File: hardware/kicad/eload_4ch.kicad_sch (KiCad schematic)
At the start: 0 parts

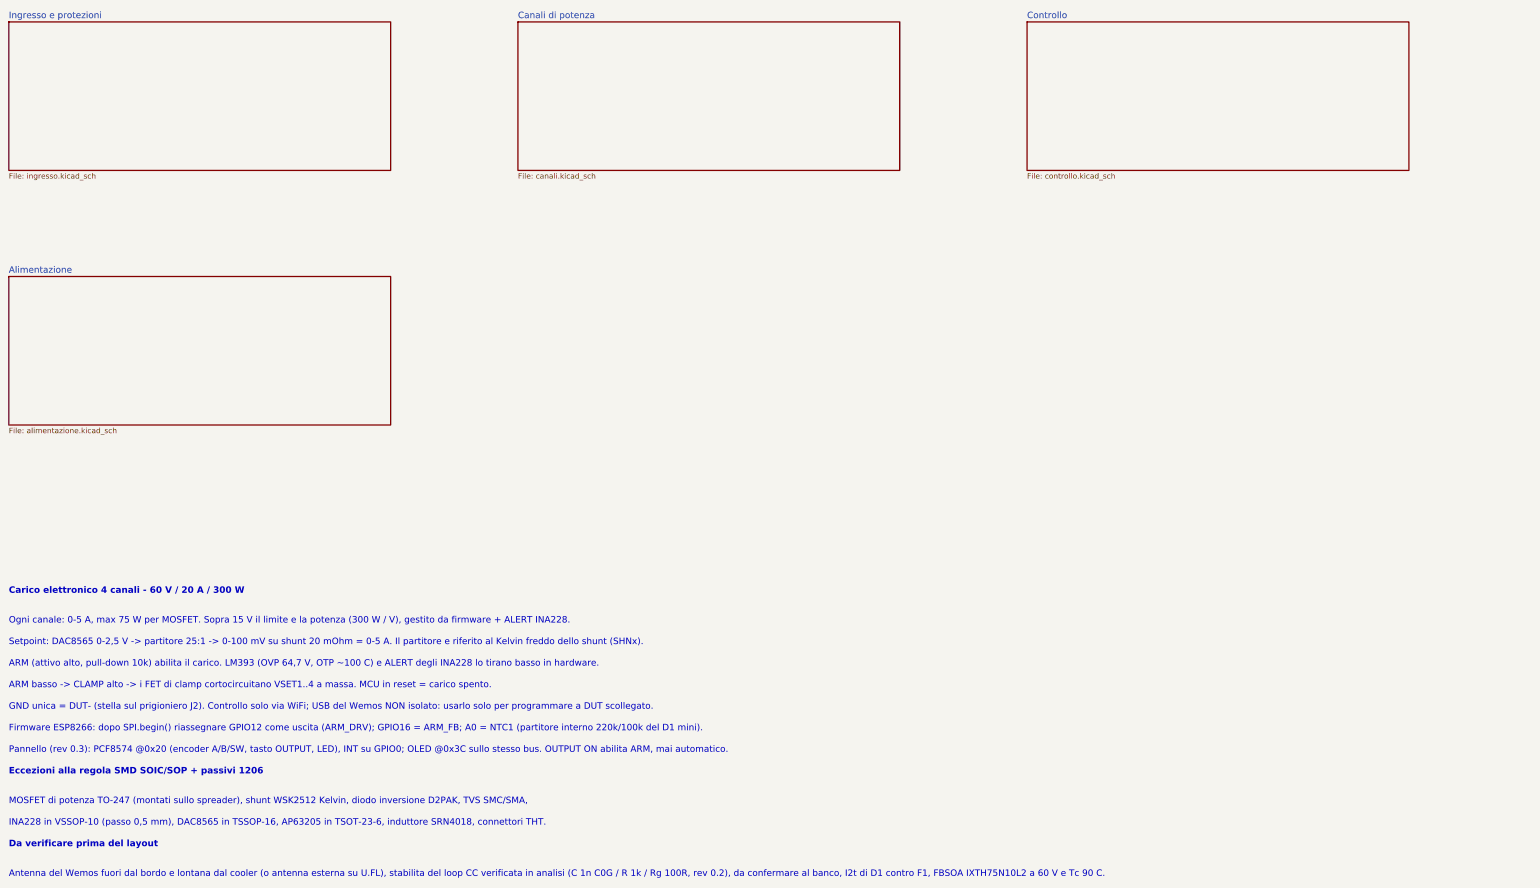
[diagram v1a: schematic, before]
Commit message: Translate schematic and PCB to English
Sheets renamed (input, channels, control, power), all titles, notes,
values and board texts in English; symbol library renamed to eload.
Re-routed board: DRC with schematic parity clean.

Co-Authored-By: Claude Opus 5.5 <noreply@anthropic.com>
Claude-Session: https://claude.ai/code/session_013KrwoEq2Y4F9LNKutY5RJ4
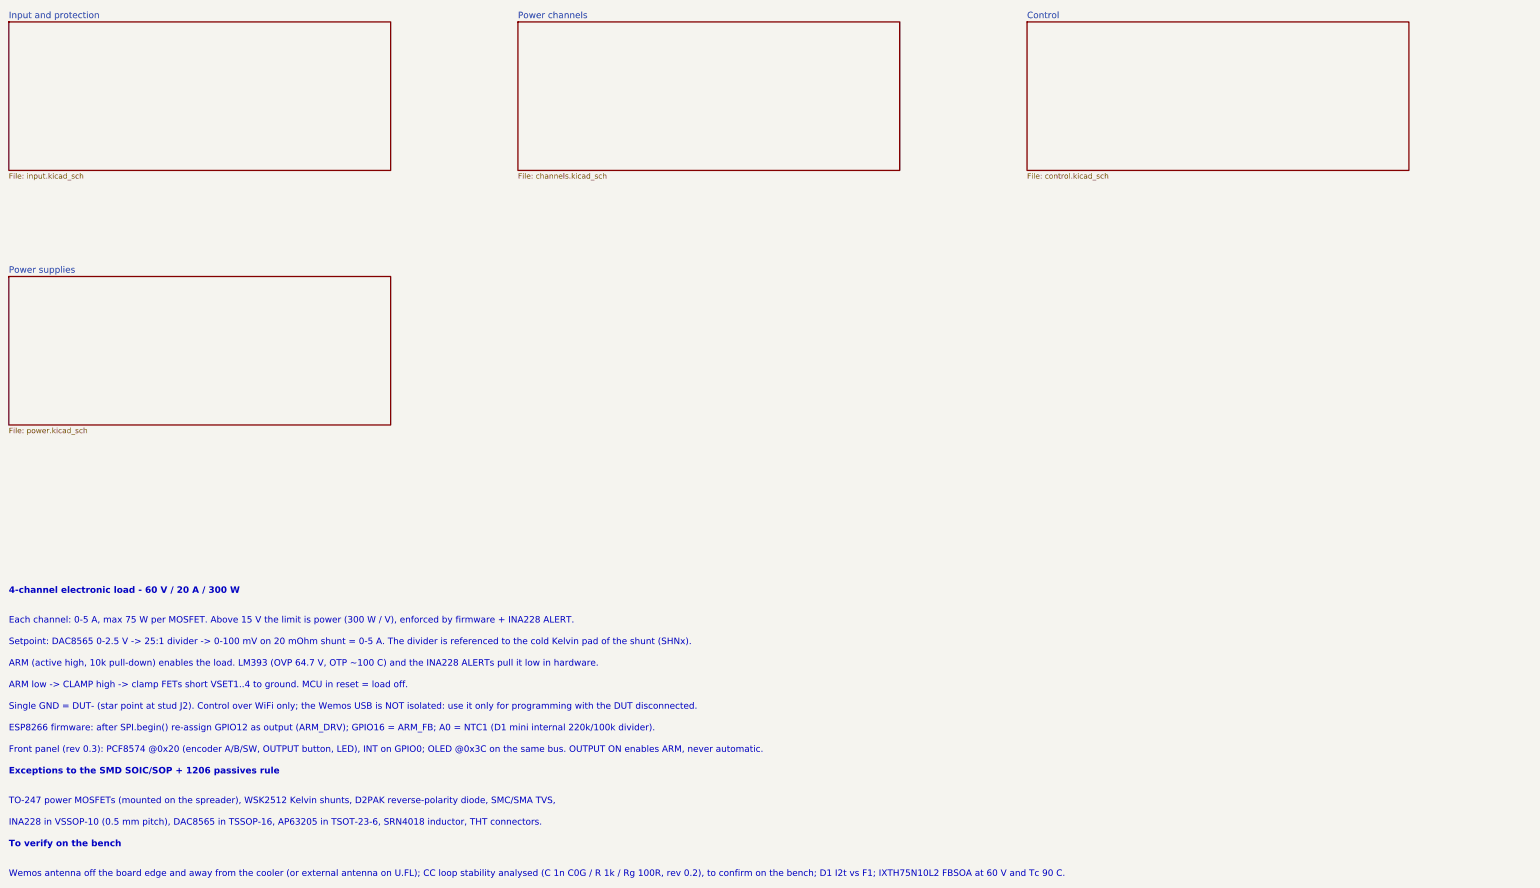
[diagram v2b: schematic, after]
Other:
- removed sheet Alimentazione
- removed sheet Canali di potenza
- removed sheet Controllo
- removed sheet Ingresso e protezioni
- added sheet Control (control.kicad_sch)
- added sheet Input and protection (input.kicad_sch)
- added sheet Power channels (channels.kicad_sch)
- added sheet Power supplies (power.kicad_sch)
- note added: "4-channel electronic load - 60 V / 20 A / 300 W"
- note added: "ARM (active high, 10k pull-down) enables the load. LM393 (OVP 64.7 V, OTP ~100 C) and the INA228 ALERTs pull it low in hardware."
- note added: "ARM low -> CLAMP high -> clamp FETs short VSET1..4 to ground. MCU in reset = load off."
- note added: "ESP8266 firmware: after SPI.begin() re-assign GPIO12 as output (ARM_DRV); GPIO16 = ARM_FB; A0 = NTC1 (D1 mini internal 220k/100k divider)."
- note added: "Each channel: 0-5 A, max 75 W per MOSFET. Above 15 V the limit is power (300 W / V), enforced by firmware + INA228 ALERT."
- note added: "Exceptions to the SMD SOIC/SOP + 1206 passives rule"
- note added: "Front panel (rev 0.3): PCF8574 @0x20 (encoder A/B/SW, OUTPUT button, LED), INT on GPIO0; OLED @0x3C on the same bus. OUTPUT ON enables ARM, never automatic."
- note added: "INA228 in VSSOP-10 (0.5 mm pitch), DAC8565 in TSSOP-16, AP63205 in TSOT-23-6, SRN4018 inductor, THT connectors."
- note added: "Setpoint: DAC8565 0-2.5 V -> 25:1 divider -> 0-100 mV on 20 mOhm shunt = 0-5 A. The divider is referenced to the cold Kelvin pad of the shunt (SHNx)."
- note added: "Single GND = DUT- (star point at stud J2). Control over WiFi only; the Wemos USB is NOT isolated: use it only for programming with the DUT disconnected."
- note added: "TO-247 power MOSFETs (mounted on the spreader), WSK2512 Kelvin shunts, D2PAK reverse-polarity diode, SMC/SMA TVS,"
- note added: "To verify on the bench"
- note added: "Wemos antenna off the board edge and away from the cooler (or external antenna on U.FL); CC loop stability analysed (C 1n C0G / R 1k / Rg 100R, rev 0.2), to confirm on the bench; D1 I2t vs F1; IXTH75N10L2 FBSOA at 60 V and Tc 90 C."
- note removed: "ARM (attivo alto, pull-down 10k) abilita il carico. LM393 (OVP 64,7 V, OTP ~100 C) e ALERT degli INA228 lo tirano basso in hardware."
- note removed: "ARM basso -> CLAMP alto -> i FET di clamp cortocircuitano VSET1..4 a massa. MCU in reset = carico spento."
- note removed: "Antenna del Wemos fuori dal bordo e lontana dal cooler (o antenna esterna su U.FL), stabilita del loop CC verificata in analisi (C 1n C0G / R 1k / Rg 100R, rev 0.2), da confermare al banco, I2t di D1 contro F1, FBSOA IXTH75N10L2 a 60 V e Tc 90 C."
- note removed: "Carico elettronico 4 canali - 60 V / 20 A / 300 W"
- note removed: "Da verificare prima del layout"
- note removed: "Eccezioni alla regola SMD SOIC/SOP + passivi 1206"
- note removed: "Firmware ESP8266: dopo SPI.begin() riassegnare GPIO12 come uscita (ARM_DRV); GPIO16 = ARM_FB; A0 = NTC1 (partitore interno 220k/100k del D1 mini)."
- note removed: "GND unica = DUT- (stella sul prigioniero J2). Controllo solo via WiFi; USB del Wemos NON isolato: usarlo solo per programmare a DUT scollegato."
- note removed: "INA228 in VSSOP-10 (passo 0,5 mm), DAC8565 in TSSOP-16, AP63205 in TSOT-23-6, induttore SRN4018, connettori THT."
- note removed: "MOSFET di potenza TO-247 (montati sullo spreader), shunt WSK2512 Kelvin, diodo inversione D2PAK, TVS SMC/SMA,"
- note removed: "Ogni canale: 0-5 A, max 75 W per MOSFET. Sopra 15 V il limite e la potenza (300 W / V), gestito da firmware + ALERT INA228."
- note removed: "Pannello (rev 0.3): PCF8574 @0x20 (encoder A/B/SW, tasto OUTPUT, LED), INT su GPIO0; OLED @0x3C sullo stesso bus. OUTPUT ON abilita ARM, mai automatico."
- note removed: "Setpoint: DAC8565 0-2,5 V -> partitore 25:1 -> 0-100 mV su shunt 20 mOhm = 0-5 A. Il partitore e riferito al Kelvin freddo dello shunt (SHNx)."
- title: Carico attivo 60V 20A 300W — Indice -> Electronic Load 4ch 60V 20A 300W — Index
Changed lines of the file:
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@@
 	(paper "A3")
 	(title_block
-		(title "Carico attivo 60V 20A 300W — Indice")
+		(title "Electronic Load 4ch 60V 20A 300W — Index")
 		(date "2026-10-25")
 		(rev "0.3")
 		(company "IV3HGA")
-		(comment 1 "Schema gerarchico: un foglio per blocco funzionale")
-	)
-	(text "GND unica = DUT- (stella sul prigioniero J2). Controllo solo via WiFi; USB del Wemos NON isolato: usarlo solo per programmare a DUT scollegato."
+		(comment 1 "Hierarchical schematic: one sheet per functional block")
+	)
+	(text "Exceptions to the SMD SOIC/SOP + 1206 passives rule"
+		(exclude_from_sim no)
+		(at 30 227.56 0)
+		(effects
+			(font
+				(size 1.524 1.524)
+				(bold yes)
+			)
+			(justify left bottom)
+		)
+	)
+	(text "INA228 in VSSOP-10 (0.5 mm pitch), DAC8565 in TSSOP-16, AP63205 in TSOT-23-6, SRN4018 inductor, THT connectors."
+		(exclude_from_sim no)
+		(at 30 239.64 0)
+		(effects
+			(font
+				(size 1.524 1.524)
+			)
+			(justify left bottom)
+		)
+	)
+	(text "4-channel electronic load - 60 V / 20 A / 300 W"
+		(exclude_from_sim no)
+		(at 30 185 0)
+		(effects
+			(font
+				(size 1.524 1.524)
+				(bold yes)
+			)
+			(justify left bottom)
+		)
+	)
+	(text "Setpoint: DAC8565 0-2.5 V -> 25:1 divider -> 0-100 mV on 20 mOhm shunt = 0-5 A. The divider is referenced to the cold Kelvin pad of the shunt (SHNx)."
+		(exclude_from_sim no)
+		(at 30 197.08 0)
+		(effects
+			(font
+				(size 1.524 1.524)
+			)
+			(justify left bottom)
+		)
+	)
+	(text "Wemos antenna off the board edge and away from the cooler (or external antenna on U.FL); CC loop stability analysed (C 1n C0G / R 1k / Rg 100R, rev 0.2), to confirm on the bench; D1 I2t vs F1; IXTH75N10L2 FBSOA at 60 V and Tc 90 C."
+		(exclude_from_sim no)
+		(at 30 251.72 0)
+		(effects
+			(font
+				(size 1.524 1.524)
+			)
+			(justify left bottom)
+		)
+	)
+	(text "ARM (active high, 10k pull-down) enables the load. LM393 (OVP 64.7 V, OTP ~100 C) and the INA228 ALERTs pull it low in hardware."
+		(exclude_from_sim no)
+		(at 30 202.16 0)
+		(effects
+			(font
+				(size 1.524 1.524)
+			)
+			(justify left bottom)
+		)
+	)
+	(text "Each channel: 0-5 A, max 75 W per MOSFET. Above 15 V the limit is power (300 W / V), enforced by firmware + INA228 ALERT."
+		(exclude_from_sim no)
+		(at 30 192 0)
+		(effects
+			(font
+				(size 1.524 1.524)
+			)
+			(justify left bottom)
+		)
+	)
+	(text "ARM low -> CLAMP high -> clamp FETs short VSET1..4 to ground. MCU in reset = load off."
+		(exclude_from_sim no)
+		(at 30 207.24 0)
+		(effects
+			(font
+				(size 1.524 1.524)
+			)
+			(justify left bottom)
+		)
+	)
+	(text "ESP8266 firmware: after SPI.begin() re-assign GPIO12 as output (ARM_DRV); GPIO16 = ARM_FB; A0 = NTC1 (D1 mini internal 220k/100k divider)."
+		(exclude_from_sim no)
+		(at 30 217.4 0)
+		(effects
+			(font
+				(size 1.524 1.524)
+			)
+			(justify left bottom)
+		)
+	)
+	(text "Front panel (rev 0.3): PCF8574 @0x20 (encoder A/B/SW, OUTPUT button, LED), INT on GPIO0; OLED @0x3C on the same bus. OUTPUT ON enables ARM, never automatic."
+		(exclude_from_sim no)
+		(at 30 222.48 0)
+		(effects
+			(font
+				(size 1.524 1.524)
+			)
+			(justify left bottom)
+		)
+	)
+	(text "To verify on the bench"
+		(exclude_from_sim no)
+		(at 30 244.72 0)
+		(effects
+			(font
+				(size 1.524 1.524)
+				(bold yes)
+			)
+			(justify left bottom)
+		)
+	)
+	(text "TO-247 power MOSFETs (mounted on the spreader), WSK2512 Kelvin shunts, D2PAK reverse-polarity diode, SMC/SMA TVS,"
+		(exclude_from_sim no)
+		(at 30 234.56 0)
+		(effects
+			(font
+				(size 1.524 1.524)
+			)
+			(justify left bottom)
+		)
+	)
+	(text "Single GND = DUT- (star point at stud J2). Control over WiFi only; the Wemos USB is NOT isolated: use it only for programming with the DUT disconnected."
 		(exclude_from_sim no)
 		(at 30 212.32 0)
-		(effects
-			(font
-				(size 1.524 1.524)
-			)
-			(justify left bottom)
-		)
-	)
-	(text "Da verificare prima del layout"
-		(exclude_from_sim no)
-		(at 30 244.72 0)
-		(effects
-			(font
-				(size 1.524 1.524)
-				(bold yes)
-			)
-			(justify left bottom)
-		)
-	)
-	(text "Pannello (rev 0.3): PCF8574 @0x20 (encoder A/B/SW, tasto OUTPUT, LED), INT su GPIO0; OLED @0x3C sullo stesso bus. OUTPUT ON abilita ARM, mai automatico."
-		(exclude_from_sim no)
-		(at 30 222.48 0)
-		(effects
-			(font
-				(size 1.524 1.524)
-			)
-			(justify left bottom)
-		)
-	)
-	(text "MOSFET di potenza TO-247 (montati sullo spreader), shunt WSK2512 Kelvin, diodo inversione D2PAK, TVS SMC/SMA,"
-		(exclude_from_sim no)
-		(at 30 234.56 0)
-		(effects
-			(font
-				(size 1.524 1.524)
-			)
-			(justify left bottom)
-		)
-	)
-	(text "INA228 in VSSOP-10 (passo 0,5 mm), DAC8565 in TSSOP-16, AP63205 in TSOT-23-6, induttore SRN4018, connettori THT."
-		(exclude_from_sim no)
-		(at 30 239.64 0)
-		(effects
-			(font
-				(size 1.524 1.524)
-			)
-			(justify left bottom)
-		)
-	)
-	(text "Setpoint: DAC8565 0-2,5 V -> partitore 25:1 -> 0-100 mV su shunt 20 mOhm = 0-5 A. Il partitore e riferito al Kelvin freddo dello shunt (SHNx)."
-		(exclude_from_sim no)
-		(at 30 197.08 0)
-		(effects
-			(font
-				(size 1.524 1.524)
-			)
-			(justify left bottom)
-		)
-	)
-	(text "ARM basso -> CLAMP alto -> i FET di clamp cortocircuitano VSET1..4 a massa. MCU in reset = carico spento."
-		(exclude_from_sim no)
-		(at 30 207.24 0)
-		(effects
-			(font
-				(size 1.524 1.524)
-			)
-			(justify left bottom)
-		)
-	)
-	(text "Firmware ESP8266: dopo SPI.begin() riassegnare GPIO12 come uscita (ARM_DRV); GPIO16 = ARM_FB; A0 = NTC1 (partitore interno 220k/100k del D1 mini)."
-		(exclude_from_sim no)
-		(at 30 217.4 0)
-		(effects
-			(font
-				(size 1.524 1.524)
-			)
-			(justify left bottom)
-		)
-	)
-	(text "Carico elettronico 4 canali - 60 V / 20 A / 300 W"
-		(exclude_from_sim no)
-		(at 30 185 0)
-		(effects
-			(font
-				(size 1.524 1.524)
-				(bold yes)
-			)
-			(justify left bottom)
-		)
-	)
-	(text "Antenna del Wemos fuori dal bordo e lontana dal cooler (o antenna esterna su U.FL), stabilita del loop CC verificata in analisi (C 1n C0G / R 1k / Rg 100R, rev 0.2), da confermare al banco, I2t di D1 contro F1, FBSOA IXTH75N10L2 a 60 V e Tc 90 C."
-		(exclude_from_sim no)
-		(at 30 251.72 0)
-		(effects
-			(font
-				(size 1.524 1.524)
-			)
-			(justify left bottom)
-		)
-	)
-	(text "Eccezioni alla regola SMD SOIC/SOP + passivi 1206"
-		(exclude_from_sim no)
-		(at 30 227.56 0)
-		(effects
-			(font
-				(size 1.524 1.524)
-				(bold yes)
-			)
-			(justify left bottom)
-		)
-	)
-	(text "ARM (attivo alto, pull-down 10k) abilita il carico. LM393 (OVP 64,7 V, OTP ~100 C) e ALERT degli INA228 lo tirano basso in hardware."
-		(exclude_from_sim no)
-		(at 30 202.16 0)
-		(effects
-			(font
-				(size 1.524 1.524)
-			)
-			(justify left bottom)
-		)
-	)
-	(text "Ogni canale: 0-5 A, max 75 W per MOSFET. Sopra 15 V il limite e la potenza (300 W / V), gestito da firmware + ALERT INA228."
-		(exclude_from_sim no)
-		(at 30 192 0)
 		(effects
 			(font
@@
 			(color 0 0 0 0)
 		)
-		(property "Sheetname" "Controllo"
+		(property "Sheetname" "Control"
 			(at 270 49.3 0)
 			(show_name no)
@@
 			)
 		)
-		(property "Sheetfile" "controllo.kicad_sch"
+		(property "Sheetfile" "control.kicad_sch"
 			(at 270 85.6 0)
 			(show_name no)
@@
 		(instances
 			(project "eload_4ch"
-				(path "/28bb9797-67af-4466-82ad-11ee221e49cb"
+				(path "/591cad4a-5508-4909-9aa0-e526f481f700"
 					(page "4")
 				)
@@
 	)
 	(sheet
-		(at 150 50)
+		(at 30 50)
 		(size 90 35)
 		(exclude_from_sim no)
@@
 			(color 0 0 0 0)
 		)
-		(property "Sheetname" "Canali di potenza"
-			(at 150 49.3 0)
+		(property "Sheetname" "Input and protection"
+			(at 30 49.3 0)
 			(show_name no)
 			(do_not_autoplace no)
@@
 			)
 		)
-		(property "Sheetfile" "canali.kicad_sch"
-			(at 150 85.6 0)
+		(property "Sheetfile" "input.kicad_sch"
+			(at 30 85.6 0)
 			(show_name no)
 			(do_not_autoplace no)
@@
 		(instances
 			(project "eload_4ch"
-				(path "/28bb9797-67af-4466-82ad-11ee221e49cb"
-					(page "3")
+				(path "/591cad4a-5508-4909-9aa0-e526f481f700"
+					(page "2")
 				)
 			)
@@
 			(color 0 0 0 0)
 		)
-		(property "Sheetname" "Alimentazione"
+		(property "Sheetname" "Power supplies"
 			(at 30 109.3 0)
 			(show_name no)
@@
 			)
 		)
-		(property "Sheetfile" "alimentazione.kicad_sch"
+		(property "Sheetfile" "power.kicad_sch"
 			(at 30 145.6 0)
 			(show_name no)
@@
 		(instances
 			(project "eload_4ch"
-				(path "/28bb9797-67af-4466-82ad-11ee221e49cb"
+				(path "/591cad4a-5508-4909-9aa0-e526f481f700"
 					(page "5")
 				)
@@
 	)
 	(sheet
-		(at 30 50)
+		(at 150 50)
 		(size 90 35)
 		(exclude_from_sim no)
@@
 			(color 0 0 0 0)
 		)
-		(property "Sheetname" "Ingresso e protezioni"
-			(at 30 49.3 0)
+		(property "Sheetname" "Power channels"
+			(at 150 49.3 0)
 			(show_name no)
 			(do_not_autoplace no)
@@
 			)
 		)
-		(property "Sheetfile" "ingresso.kicad_sch"
-			(at 30 85.6 0)
+		(property "Sheetfile" "channels.kicad_sch"
+			(at 150 85.6 0)
 			(show_name no)
 			(do_not_autoplace no)
@@
 		(instances
 			(project "eload_4ch"
-				(path "/28bb9797-67af-4466-82ad-11ee221e49cb"
-					(page "2")
-				)
-			)
+				(path "/591cad4a-5508-4909-9aa0-e526f481f700"
+					(page "3")
+				)
+			)
